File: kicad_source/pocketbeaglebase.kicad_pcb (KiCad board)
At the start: 2 copper layers, 100 x 60 mm, 95 parts, among them J1 RJ45-TRANSFO-2, P1 USB_2.0_Connector, P10 CONN_01X03, P11 CONN_01X02, P2 CONN_01X03, P3 CONN_01X04, P4 CONN_02X20, P5 CONN_01X04, P6 CONN_01X04, P7 CONN_01X04, P8 CONN_02X03, P9 WR-TBL_691322310002, SW1 SW_PUSH, U1 BEAGLE_PocketBeagle, U2 LAN9514, U3 MIC2026, U4 MAX3227, U5 93LC66, U6 TPS54335A, U7 SN65HVD232, Y1 25MHz

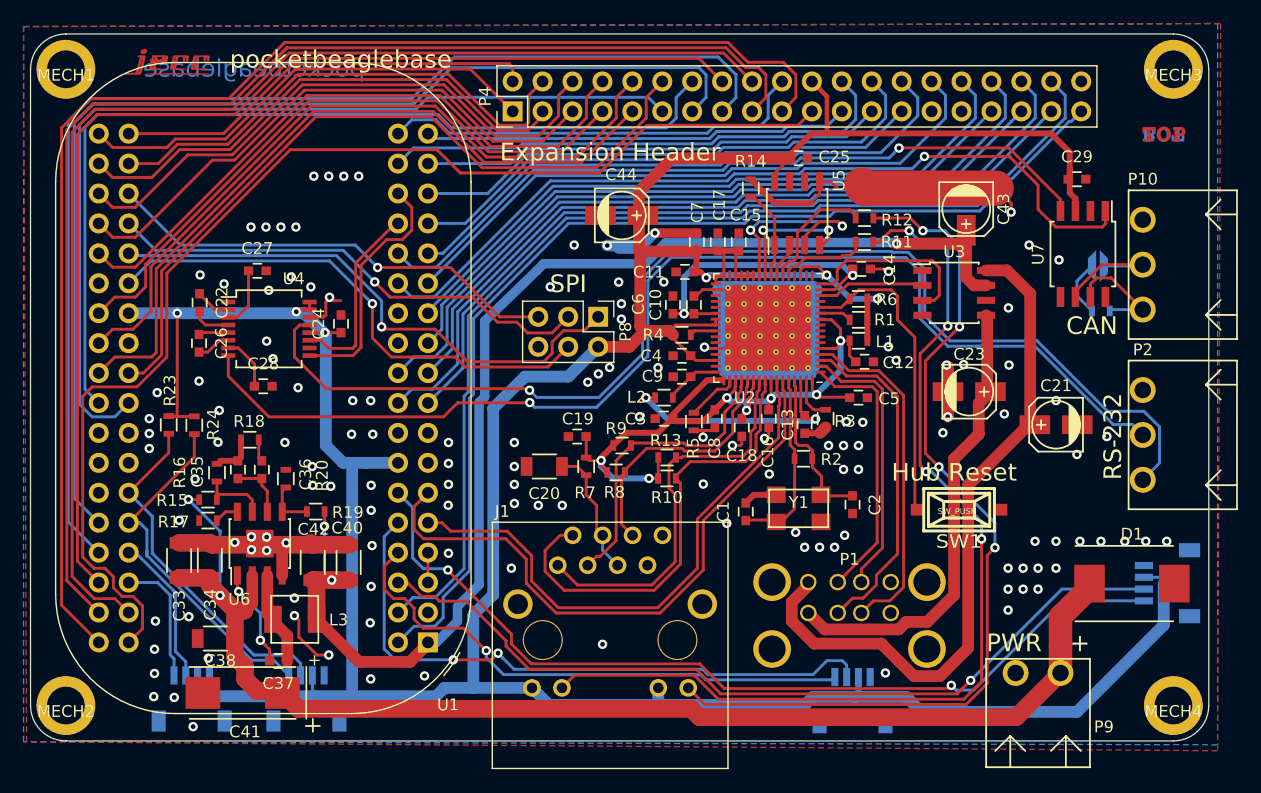
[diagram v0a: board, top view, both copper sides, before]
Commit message: tested and fixed last bugs
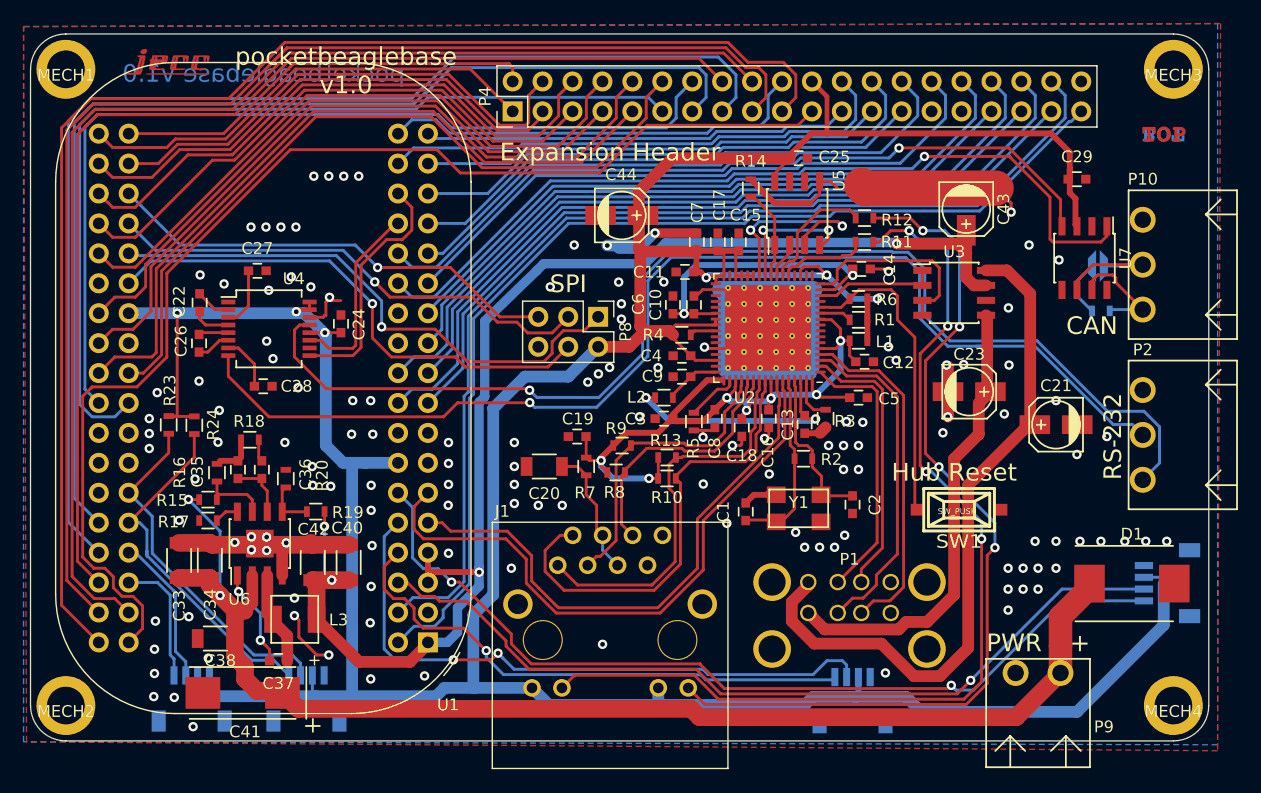
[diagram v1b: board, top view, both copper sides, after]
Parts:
- R1: value 10k -> 1k
- U7: footprint SOIC:SOIJ-8_5.3x5.3mm_Pitch1.27mm -> SOIC:SOIC-8_3.9x4.9mm_Pitch1.27mm
- moved U7 0.37 mm to (179.4, 59.0)
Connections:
- U1 pad 5: USB_VBUS -> +5V
- U1 pad 7: USB_VBUS -> +5V
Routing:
- net +5V: track 103.9 -> 111.7 mm, vias 3 -> 4
- net USB_VBUS: track 2.54 -> 0.00 mm
- net CAN0_RX: track 63.7 -> 65.3 mm
- net CAN0_TX: track 70.4 -> 71.8 mm
- net +3V3: track 329.3 -> 330.7 mm
- net /nIO89: track 89.9 -> 90.6 mm
- net /UART/nCANH: track 9.71 -> 10.2 mm
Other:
- board text added: "pocketbeaglebase v1.0"
- board text removed: "pocketbeaglebase"
